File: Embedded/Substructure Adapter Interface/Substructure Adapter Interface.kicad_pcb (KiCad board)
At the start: 2 copper layers, 26.8 x 16 mm, 3 parts, among them J1 Conn_01x02_Socket, J2 Conn_02x10_Odd_Even

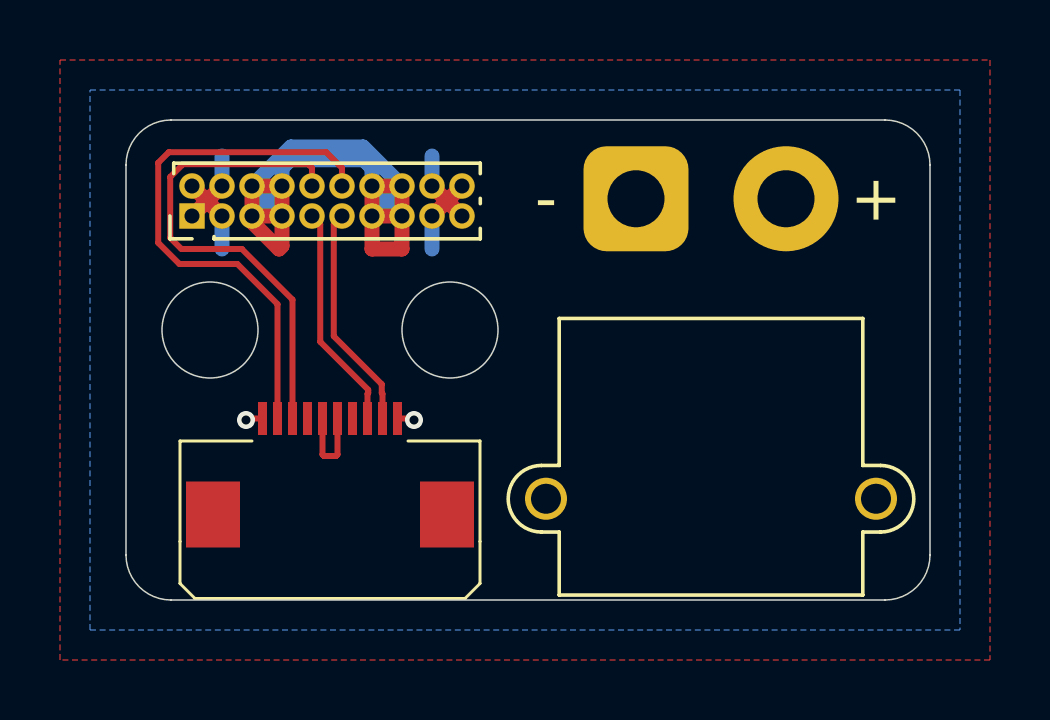
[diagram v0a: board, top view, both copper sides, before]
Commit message: Modified Ports to fit FFC orientations
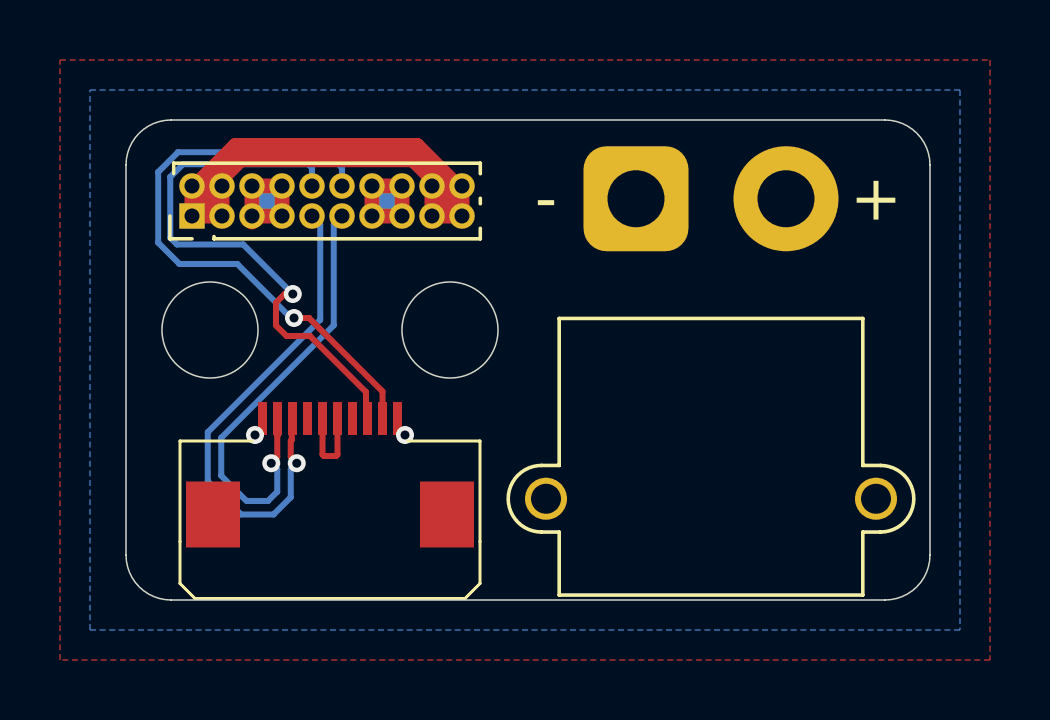
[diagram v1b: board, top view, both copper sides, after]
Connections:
- U1 pad 2: Power UART RX -> Power USB -
- U1 pad 3: Power UART TX -> Power USB +
- U1 pad 4: Power GPIO 0 -> Power GPIO 1
- U1 pad 7: Power GPIO 1 -> Power GPIO 0
- U1 pad 8: Power USB + -> Power UART TX
- U1 pad 9: Power USB - -> Power UART RX
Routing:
- net GND: track 11.0 -> 33.1 mm
- net +RAWVS: track 32.9 -> 16.8 mm
- net Power USB +: track 7.54 -> 16.8 mm, vias 0 -> 1
- net Power USB -: track 7.54 -> 15.3 mm, vias 0 -> 1
- net Power UART TX: track 16.5 -> 18.7 mm, vias 0 -> 1
- net Power UART RX: track 18.4 -> 20.0 mm, vias 0 -> 1

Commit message: Added Logos
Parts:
- added G***: LOGO, LOGO, B.Cu at (117.5, 70.0)
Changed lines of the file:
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@@
+		(embedded_fonts no)
+	)
+	(footprint "LOGO"
+		(layer "B.Cu")
+		(at 117.5 70 180)
+		(property "Reference" "G***"
+			(at 0 0 0)
+			(layer "B.SilkS")
+			(hide yes)
+			(effects
+				(font
+					(size 1.5 1.5)
+					(thickness 0.3)
+				)
+				(justify mirror)
+			)
+		)
+		(property "Value" "LOGO"
+			(at 0.75 0 0)
+			(layer "B.SilkS")
+			(hide yes)
+			(effects
+				(font
+					(size 1.5 1.5)
+					(thickness 0.3)
+				)
+				(justify mirror)
+			)
+		)
+		(property "Datasheet" ""
+			(at 0 0 0)
+			(layer "B.Fab")
+			(hide yes)
+			(effects
+				(font
+					(size 1.27 1.27)
+					(thickness 0.15)
+				)
+				(justify mirror)
+			)
+		)
+		(property "Description" ""
+			(at 0 0 0)
+			(layer "B.Fab")
+			(hide yes)
+			(effects
+				(font
+					(size 1.27 1.27)
+					(thickness 0.15)
+				)
+				(justify mirror)
+			)
+		)
+		(attr board_only exclude_from_pos_files exclude_from_bom)
+		(fp_poly
+			(pts
+				(xy 2.297355 1.399853) (xy 2.425981 1.233782) (xy 2.594527 0.988878) (xy 2.786639 0.691264) (xy 2.985966 0.367064)
+				(xy 3.176156 0.042399) (xy 3.340856 -0.256606) (xy 3.463716 -0.503829) (xy 3.484683 -0.551435) (xy 3.632319 -0.932866)
+				(xy 3.769731 -1.349654) (xy 3.885568 -1.76073) (xy 3.968482 -2.125024) (xy 4.007121 -2.401464) (xy 4.008554 -2.447088)
+				(xy 3.982905 -2.594393) (xy 3.896406 -2.648933) (xy 3.734726 -2.608779) (xy 3.483536 -2.472004)
+				(xy 3.296754 -2.351368) (xy 2.775785 -2.031367) (xy 2.284269 -1.783532) (xy 1.850089 -1.620751)
+				(xy 1.593489 -1.564083) (xy 1.300882 -1.505648) (xy 1.153337 -1.419241) (xy 1.146859 -1.292318)
+				(xy 1.277452 -1.112333) (xy 1.408737 -0.983902) (xy 1.785575 -0.55174) (xy 2.032278 -0.060547) (xy 2.155084 0.50461)
+				(xy 2.172078 0.842826) (xy 2.178265 1.125944) (xy 2.194061 1.340863) (xy 2.216473 1.452656) (xy 2.224999 1.460968)
+			)
+			(stroke
+				(width 0)
+				(type solid)
+			)
+			(fill yes)
+			(layer "B.SilkS")
+		)
+		(fp_poly
+			(pts
+				(xy -0.080498 2.793867) (xy 0.291311 2.759704) (xy 0.587531 2.694994) (xy 0.832749 2.593627) (xy 1.051554 2.449489)
+				(xy 1.268535 2.25647) (xy 1.351314 2.173453) (xy 1.629065 1.843441) (xy 1.802448 1.509869) (xy 1.889951 1.124665)
+				(xy 1.910619 0.719433) (xy 1.874321 0.272492) (xy 1.751872 -0.095506) (xy 1.522938 -0.440243) (xy 1.460158 -0.514064)
+				(xy 1.071066 -0.872589) (xy 0.639858 -1.096508) (xy 0.136236 -1.200339) (xy 0.01081 -1.208593) (xy -0.28665 -1.211925)
+				(xy -0.548701 -1.197744) (xy -0.716176 -1.169687) (xy -0.970994 -1.068617) (xy -1.219156 -0.925512)
+				(xy -1.503404 -0.713589) (xy -1.685842 -0.56205) (xy -2.035598 -0.28027) (xy -2.350653 -0.070026)
+				(xy -2.686801 0.100164) (xy -3.09984 0.261782) (xy -3.22183 0.304598) (xy -3.50878 0.408231) (xy -3.746001 0.502084)
+				(xy -3.893486 0.570061) (xy -3.914898 0.58349) (xy -3.991925 0.729281) (xy -3.993518 0.778936) (xy -0.785061 0.778936)
+				(xy -0.723776 0.487191) (xy -0.558521 0.268436) (xy -0.323182 0.136914) (xy -0.051644 0.106867)
+				(xy 0.222207 0.192536) (xy 0.363689 0.296128) (xy 0.528523 0.538856) (xy 0.573961 0.818218) (xy 0.507321 1.09203)
+				(xy 0.335916 1.318106) (xy 0.168648 1.420805) (xy -0.136928 1.479431) (xy -0.414389 1.408777) (xy -0.633194 1.229397)
+				(xy -0.762805 0.961845) (xy -0.785061 0.778936) (xy -3.993518 0.778936) (xy -3.999554 0.96714) (xy -3.946933 1.261518)
+				(xy -3.843211 1.576864) (xy -3.697536 1.877631) (xy -3.519057 2.128267) (xy -3.51668 2.130906) (xy -3.290422 2.331536)
+				(xy -3.00711 2.518533) (xy -2.865304 2.59051) (xy -2.706517 2.654574) (xy -2.544772 2.701979) (xy -2.352391 2.736022)
+				(xy -2.101697 2.760002) (xy -1.765009 2.777217) (xy -1.314651 2.790965) (xy -1.149238 2.795) (xy -0.552485 2.803595)
+			)
+			(stroke
+				(width 0)
+				(type solid)
+			)
+			(fill yes)
+			(layer "B.SilkS")
+		)
 		(embedded_fonts no)
 	)
